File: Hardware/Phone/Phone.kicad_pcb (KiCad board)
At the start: 2 copper layers, 16.5 x 1.9 mm, 24 parts, among them J1 UART, J2 JTAG, J3 USB_C_Receptacle_USB2.0_16P, U1 ESP32-S3-WROOM-1, U2 USBLC6-2SC6

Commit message: e ink is done
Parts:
- added C10: 10p, Capacitor_SMD:C_0603_1608Metric, F.Cu at (136.4, 53.5)
- added C11: 10p, Capacitor_SMD:C_0603_1608Metric, F.Cu at (136.4, 56.1)
- added C12: 10p, Capacitor_SMD:C_0603_1608Metric, F.Cu at (136.4, 58.6)
- added C13: 33p, Capacitor_SMD:C_0603_1608Metric, F.Cu at (136.4, 61.1)
- added C14: 10p, Capacitor_SMD:C_0603_1608Metric, F.Cu at (140.4, 43.5)
- added C15: 33p, Capacitor_SMD:C_0603_1608Metric, F.Cu at (140.4, 46.0)
- added C16: 10p, Capacitor_SMD:C_0603_1608Metric, F.Cu at (140.4, 48.5)
- added C17: 33p, Capacitor_SMD:C_0603_1608Metric, F.Cu at (140.4, 51.0)
- added C18: 10p, Capacitor_SMD:C_0603_1608Metric, F.Cu at (140.4, 53.5)
- added C19: 33p, Capacitor_SMD:C_0603_1608Metric, F.Cu at (140.4, 56.1)
- added C20: 10p, Capacitor_SMD:C_0603_1608Metric, F.Cu at (140.4, 58.6)
- added C21: 33p, Capacitor_SMD:C_0603_1608Metric, F.Cu at (140.4, 61.1)
- added C22: 10p, Capacitor_SMD:C_0603_1608Metric, F.Cu at (144.4, 43.5)
- added C23: 33p, Capacitor_SMD:C_0603_1608Metric, F.Cu at (144.4, 46.0)
- added C24: 100n, Capacitor_SMD:C_0603_1608Metric, F.Cu at (144.4, 48.5)
- added C25: 22p, Capacitor_SMD:C_0603_1608Metric, F.Cu at (144.4, 51.0)
- added C26: 22p, Capacitor_SMD:C_0603_1608Metric, F.Cu at (144.4, 53.5)
- added C27: 22p, Capacitor_SMD:C_0603_1608Metric, F.Cu at (144.4, 56.1)
- added C28: 1u, Capacitor_SMD:C_0603_1608Metric, F.Cu at (144.4, 58.6)
- added C29: 1nF, Capacitor_SMD:C_1206_3216Metric, F.Cu at (151.2, 78.8)
- added C30: ~, Capacitor_SMD:C_0603_1608Metric, F.Cu at (144.4, 61.1)
- added C31: ~, Capacitor_SMD:C_0603_1608Metric, F.Cu at (148.4, 43.5)
- added C32: 1uF, Capacitor_SMD:C_0603_1608Metric, F.Cu at (143.1, 87.1)
- added C33: 1uF, Capacitor_SMD:C_0603_1608Metric, F.Cu at (143.1, 89.6)
- added C34: 1uF, Capacitor_SMD:C_0603_1608Metric, F.Cu at (143.1, 92.1)
- added C35: 1uF, Capacitor_SMD:C_0603_1608Metric, F.Cu at (143.1, 94.6)
- added C36: 1uF, Capacitor_SMD:C_0603_1608Metric, F.Cu at (147.2, 87.1)
- added C37: 1uF, Capacitor_SMD:C_0603_1608Metric, F.Cu at (147.2, 89.6)
- added C38: 1uF, Capacitor_SMD:C_0603_1608Metric, F.Cu at (147.2, 92.1)
- added C39: 4u7, Capacitor_SMD:C_0603_1608Metric, F.Cu at (147.2, 94.6)
- added C40: 1uF, Capacitor_SMD:C_0603_1608Metric, F.Cu at (151.2, 87.1)
- added C41: 4u7, Capacitor_SMD:C_0603_1608Metric, F.Cu at (151.2, 89.6)
- added C5: 10uF, Capacitor_SMD:C_0603_1608Metric, F.Cu at (93.3, 111.1)
- added C6: 33p, Capacitor_SMD:C_0603_1608Metric, F.Cu at (136.4, 43.5)
- added C7: 33p, Capacitor_SMD:C_0603_1608Metric, F.Cu at (136.4, 46.0)
- added C8: 33p, Capacitor_SMD:C_0603_1608Metric, F.Cu at (136.4, 48.5)
- added C9: 10p, Capacitor_SMD:C_0603_1608Metric, F.Cu at (136.4, 51.0)
- added CARD1: ~, Felix_GSM:SIM-SMD_503960-0696, F.Cu at (124.1, 73.6)
- added D1: ~, Felix:SOD-882_L1.0-W0.6-BI, F.Cu at (151.8, 64.3)
- added D2: ~, Felix:SOD-882_L1.0-W0.6-BI, F.Cu at (151.8, 66.2)
- added D3: ~, Felix:SOD-882_L1.0-W0.6-BI, F.Cu at (151.8, 68.1)
- added D4: ~, Felix:SOD-882_L1.0-W0.6-BI, F.Cu at (151.8, 70.0)
- added D5: ESDA6V1-5W6, Package_TO_SOT_SMD:SOT-363_SC-70-6, F.Cu at (139.9, 81.9)
- added D6: ~, Felix:SOD-882_L1.0-W0.6-BI, F.Cu at (151.8, 71.9)
- added D7: D, Diode_SMD:D_SOD-123, F.Cu at (144.1, 97.6)
- added D8: D, Diode_SMD:D_SOD-123, F.Cu at (144.1, 100.9)
- added D9: D, Diode_SMD:D_SOD-123, F.Cu at (144.1, 104.3)
- added F2: 500mA PTC, Fuse:Fuse_1206_3216Metric_Pad1.42x1.75mm_HandSolder, F.Cu at (151.4, 75.5)
- added J4: Conn_Coaxial, Connector_Coaxial:U.FL_Hirose_U.FL-R-SMT-1_Vertical, F.Cu at (93.8, 104.0)
- added J5: Conn_Coaxial, Connector_Coaxial:U.FL_Hirose_U.FL-R-SMT-1_Vertical, F.Cu at (140.3, 76.9)
- added J6: Conn_01x02_Socket, Connector_PinHeader_2.54mm:PinHeader_1x02_P2.54mm_Vertical, F.Cu at (135.5, 76.2)
- added J7: USB_C_Receptacle_USB2.0_16P, Connector_USB:USB_C_Receptacle_HRO_TYPE-C-31-M-12, F.Cu at (139.0, 69.2)
- added L1: 47nH, Inductor_SMD:L_0805_2012Metric, F.Cu at (93.5, 108.4)
- added L2: 47u, Felix:IND-SMD_L4.0-W4.0 MNR4012, F.Cu at (149.8, 98.6)
- added Q1: Si1308EDL, Package_TO_SOT_SMD:SOT-323_SC-70, F.Cu at (149.2, 103.2)
- added R11: 22R, Resistor_SMD:R_0603_1608Metric, F.Cu at (148.4, 46.0)
- added R12: 22R, Resistor_SMD:R_0603_1608Metric, F.Cu at (148.4, 48.5)
- added R13: 5k1, Resistor_SMD:R_1206_3216Metric, F.Cu at (147.6, 65.0)
- added R14: 5k1, Resistor_SMD:R_1206_3216Metric, F.Cu at (147.6, 68.3)
- added R15: 1M, Resistor_SMD:R_1206_3216Metric, F.Cu at (147.6, 71.6)
- added R16: 1K, Resistor_SMD:R_0603_1608Metric, F.Cu at (148.4, 51.0)
- added R17: 5k6, Resistor_SMD:R_0603_1608Metric, F.Cu at (148.4, 53.5)
- added R18: 1K, Resistor_SMD:R_0603_1608Metric, F.Cu at (148.4, 56.1)
- added R19: 1K, Resistor_SMD:R_0603_1608Metric, F.Cu at (148.4, 58.6)
- added R20: 5k6, Resistor_SMD:R_0603_1608Metric, F.Cu at (148.4, 61.1)
- added R21: 4k7, Resistor_SMD:R_0603_1608Metric, F.Cu at (152.4, 43.5)
- added R22: 51R, Resistor_SMD:R_0603_1608Metric, F.Cu at (152.4, 46.0)
- added R23: 51R, Resistor_SMD:R_0603_1608Metric, F.Cu at (152.4, 48.5)
- added R24: 51R, Resistor_SMD:R_0603_1608Metric, F.Cu at (152.4, 51.0)
- added R25: 0R, Resistor_SMD:R_0603_1608Metric, F.Cu at (152.4, 53.5)
- added R26: 1M, Resistor_SMD:R_0603_1608Metric, F.Cu at (151.2, 92.1)
- added R27: 2R2, Resistor_SMD:R_0603_1608Metric, F.Cu at (151.2, 94.6)
- added TP1: TestPoint, TestPoint:TestPoint_Pad_D1.0mm, F.Cu at (149.9, 82.0)
- added U4: ~, Felix_GPS:GPSM-SMD_ATGM336H-TR, F.Cu at (85.6, 107.8)
- added U5: USBLC6-2SC6, Package_TO_SOT_SMD:SOT-23-6, F.Cu at (145.7, 81.5)
- added U7: ~, Felix:MIC-TH_BD4.0-P1.40_KEEG1542PBL-A, F.Cu at (145.3, 76.5)
- added U8: ~, Felix:GDEY027T91-T01 Eink Touch LONG, F.Cu at (140.4, 104.5)
- U6: value ~ -> SIM800C; footprint Felix_GPS:GPSM-SMD_ATGM336H-TR -> RF_GSM:SIMCom_SIM800C
- moved U6 64.7 mm to (124.8, 52.8)
- moved R9 41.5 mm to (62.5, 109.4)
- moved C4 41.5 mm to (95.0, 96.6)
- moved J1 41.5 mm to (68.5, 88.2)
- moved J2 41.5 mm to (68.5, 95.4)
- moved J3 41.5 mm to (98.0, 90.3)
- moved R10 41.5 mm to (62.5, 112.3)
- moved R6 41.5 mm to (106.7, 86.1)
- moved R7 41.5 mm to (106.7, 89.4)
- moved R8 41.5 mm to (106.7, 92.7)
- moved S1 41.5 mm to (78.5, 86.0)
- moved S2 41.5 mm to (86.1, 86.0)
- moved U1 41.5 mm to (84.6, 70.5)
- moved U2 41.5 mm to (79.6, 96.5)
- moved C2 41.5 mm to (111.1, 46.0)
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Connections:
- U6 pad 1: unconnected-(U6-GND-Pad1) -> Net-(U6-UART1_TXD)
- U6 pad 10: unconnected-(U6-GND-Pad10) -> Net-(D4-C)
- U6 pad 11: unconnected-(U6-RF_IN-Pad11) -> Net-(D2-C)
- U6 pad 12: unconnected-(U6-GND-Pad12) -> Net-(D1-A)
- U6 pad 13: unconnected-(U6-NC-Pad13) -> GND
- U6 pad 14: unconnected-(U6-VCC_RF-Pad14) -> Net-(CARD1-DETECT)
- U6 pad 15: unconnected-(U6-Reserved-Pad15) -> Net-(U6-SIM_DATA)
- U6 pad 16: unconnected-(U6-SDA-Pad16) -> Net-(U6-SIM_CLK)
- U6 pad 17: unconnected-(U6-SCL-Pad17) -> Net-(U6-SIM_RST)
- U6 pad 18: unconnected-(U6-Reserved-Pad18) -> Net-(CARD1-VCC)
- U6 pad 2: unconnected-(U6-TXD-Pad2) -> Net-(U6-UART1_RXD)
- U6 pad 6: unconnected-(U6-VBAT-Pad6) -> Net-(U6-UART1_DTR)
- U6 pad 8: unconnected-(U6-VCC-Pad8) -> GND
- U6 pad 9: unconnected-(U6-NRESET-Pad9) -> Net-(D3-A)

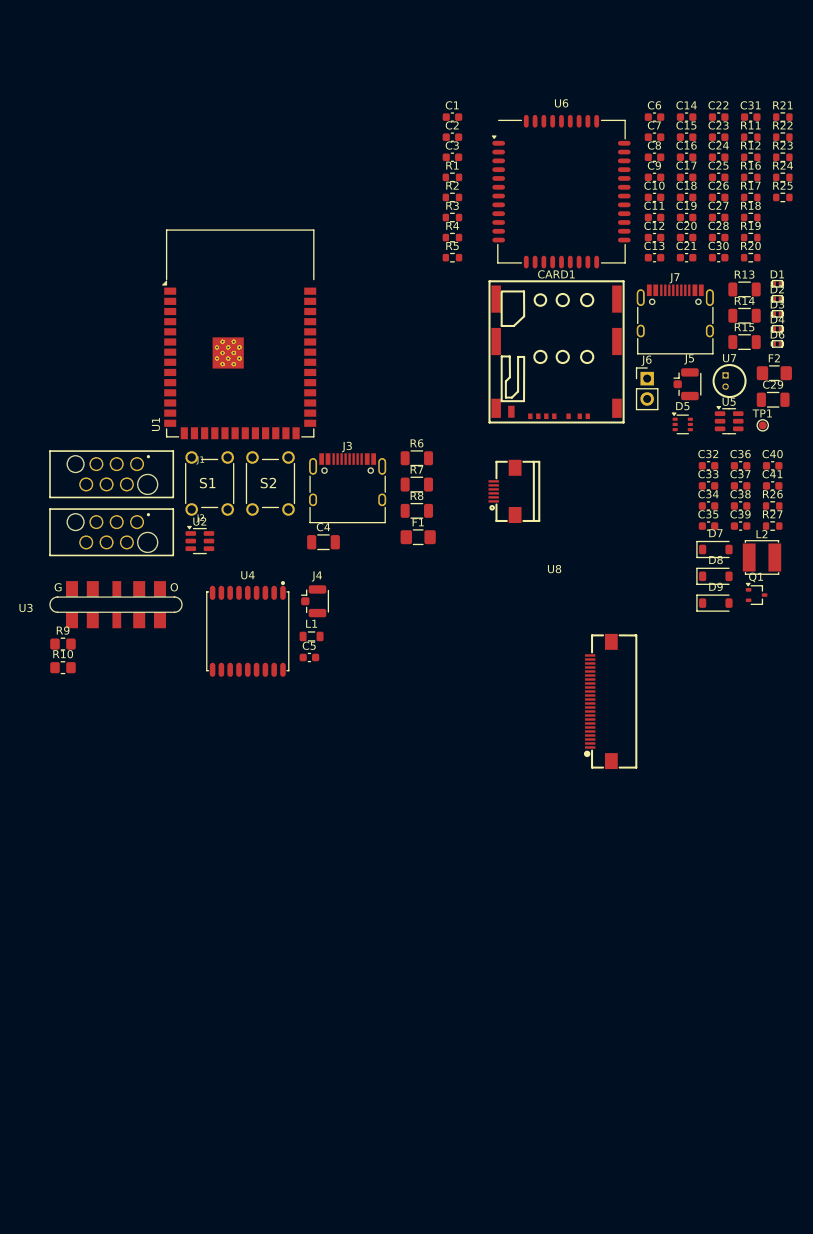
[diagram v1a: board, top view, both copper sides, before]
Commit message: phone design is done abendoning projekt
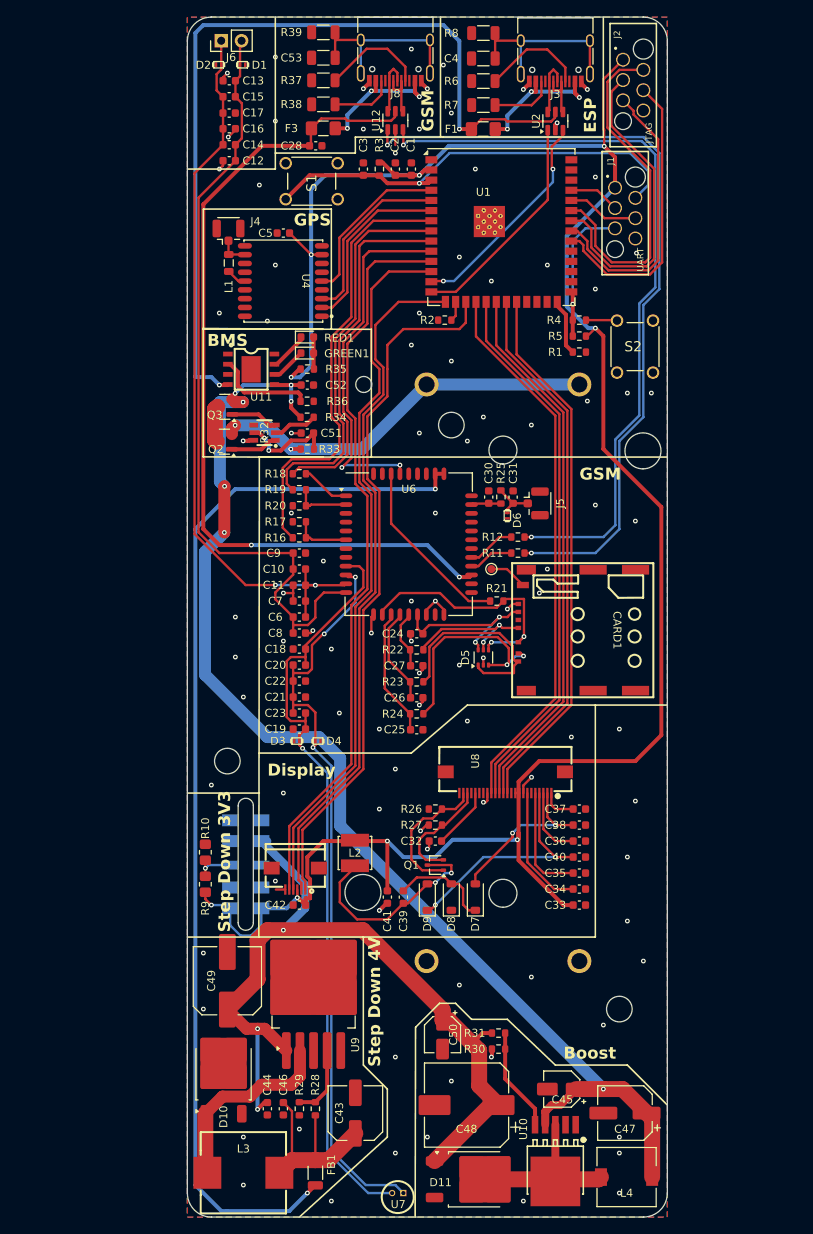
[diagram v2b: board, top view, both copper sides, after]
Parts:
- removed C29: 1nF, Capacitor_SMD:C_1206_3216Metric
- removed F2: 500mA PTC, Fuse:Fuse_1206_3216Metric_Pad1.42x1.75mm_HandSolder
- removed J7: USB_C_Receptacle_USB2.0_16P, Connector_USB:USB_C_Receptacle_HRO_TYPE-C-31-M-12
- removed R13, R14: 5k1, Resistor_SMD:R_1206_3216Metric
- removed R15: 1M, Resistor_SMD:R_1206_3216Metric
- removed U5: USBLC6-2SC6, Package_TO_SOT_SMD:SOT-23-6
- added BAT1: ~, Felix:BAT-TH_L77.0-W39.9_BH-18650-A1BJ021, B.Cu at (117.5, 113.0)
- added C42: 1uF, Capacitor_SMD:C_0603_1608Metric, F.Cu at (92.0, 142.0)
- added C43: 330u, Capacitor_SMD:C_Elec_6.3x7.7, F.Cu at (99.0, 168.0)
- added C44: 1u, Capacitor_SMD:C_0603_1608Metric, F.Cu at (88.0, 167.5)
- added C45: 10uF, Capacitor_SMD:CP_Elec_4x5.4, F.Cu at (124.8, 165.0)
- added C46: 100n, Capacitor_SMD:C_0603_1608Metric, F.Cu at (90.0, 167.5)
- added C47: 47uF, Capacitor_SMD:CP_Elec_6.3x7.7, F.Cu at (132.7, 168.0)
- added C48: 22uF, Capacitor_SMD:CP_Elec_10x10, F.Cu at (112.9, 167.0)
- added C49: 100u, Capacitor_SMD:C_Elec_8x10.2, F.Cu at (83.0, 151.5)
- added C50: 10uF, Capacitor_SMD:CP_Elec_4x5.4, F.Cu at (109.9, 158.2)
- added C51: 0u1, Capacitor_SMD:C_0603_1608Metric, F.Cu at (93.0, 83.0)
- added C52: 10uF, Capacitor_SMD:C_0603_1608Metric, F.Cu at (93.0, 77.0)
- added C53: 1nF, Capacitor_SMD:C_1206_3216Metric, F.Cu at (95.0, 36.1)
- added D10: MBR360, Package_TO_SOT_SMD:TO-252-2, F.Cu at (82.5, 163.0)
- added D11: MBR360, Package_TO_SOT_SMD:TO-252-2, F.Cu at (113.9, 176.3)
- added F3: 2A PTC, Fuse:Fuse_1206_3216Metric_Pad1.42x1.75mm_HandSolder, F.Cu at (95.0, 44.9)
- added FB1: FerriteBead 270R @ 100Mhz, Inductor_SMD:L_1206_3216Metric, F.Cu at (94.0, 175.5)
- added GREEN1: LED, LED_SMD:LED_0603_1608Metric, F.Cu at (93.0, 73.0)
- added H3: MountingHole, MountingHole:MountingHole_3.2mm_M3, F.Cu at (83.0, 124.0)
- added H4: MountingHole, MountingHole:MountingHole_3.2mm_M3, F.Cu at (111.0, 82.0)
- added H5: MountingHole, MountingHole:MountingHole_3.2mm_M3, F.Cu at (132.0, 155.0)
- added J8: USB_C_Receptacle_USB2.0_16P, Connector_USB:USB_C_Receptacle_HRO_TYPE-C-31-M-12, F.Cu at (104.0, 34.9)
- added L3: 100u, Felix:IND-SMD_L10.6-W10.2 2A 11x10mm, F.Cu at (85.0, 175.5)
- added L4: 33u, Inductor_SMD:L_7.3x7.3_H4.5, F.Cu at (132.9, 176.0)
- added Q2: AO3400A, Package_TO_SOT_SMD:SOT-23, F.Cu at (82.6, 84.1)
- added Q3: AO3400A, Package_TO_SOT_SMD:SOT-23, F.Cu at (82.7, 79.7)
- added R28: 2k2, Resistor_SMD:R_0603_1608Metric, F.Cu at (94.0, 167.5)
- added R29: 1k, Resistor_SMD:R_0603_1608Metric, F.Cu at (92.0, 167.5)
- added R30: 1k, Resistor_SMD:R_0603_1608Metric, F.Cu at (116.9, 160.0)
- added R31: 8k2, Resistor_SMD:R_0603_1608Metric, F.Cu at (116.9, 158.0)
- added R32: ~, Felix:SOT-23-6_L2.9-W1.6-P0.95-LS2.8-BR FM2113, F.Cu at (87.7, 83.0)
- added R33: 100R, Resistor_SMD:R_0603_1608Metric, F.Cu at (93.0, 85.0)
- added R34: 2K, Resistor_SMD:R_0603_1608Metric, F.Cu at (93.0, 81.0)
- added R35: 2K, Resistor_SMD:R_0603_1608Metric, F.Cu at (93.0, 75.0)
- added R36: 1K, Resistor_SMD:R_0603_1608Metric, F.Cu at (93.0, 79.0)
- added R37: 5k1, Resistor_SMD:R_1206_3216Metric, F.Cu at (95.0, 38.9)
- added R38: 5k1, Resistor_SMD:R_1206_3216Metric, F.Cu at (95.0, 41.9)
- added R39: 1M, Resistor_SMD:R_1206_3216Metric, F.Cu at (95.0, 32.9)
- added RED1: LED, LED_SMD:LED_0603_1608Metric, F.Cu at (93.0, 71.0)
- added U10: ~, Felix:TO-252-5_L6.6-W5.8-P1.27-TL XL6008E1, F.Cu at (124.0, 173.0)
- added U11: ~, Felix:ESOP-8_L4.9-W3.9-P1.27-LS6.0-BL-EP, F.Cu at (86.0, 75.0)
- added U12: USBLC6-2SC6, Package_TO_SOT_SMD:SOT-23-6, F.Cu at (104.0, 43.9)
- added U9: LM2596S-ADJ, Package_TO_SOT_SMD:TO-263-5_TabPin3, F.Cu at (93.8, 152.5)
- D1, D2, D3, D4: value ~ -> H5VL10B
- F1: value 500mA PTC -> 2A PTC
- U1: footprint RF_Module:ESP32-S3-WROOM-1 -> RF_Module:ESP32-S3-WROOM-1U
- U3: moved to B.Cu
- moved U7 109.5 mm to (104.3, 178.0), turned to -90 degrees
- moved C22 87.8 mm to (92.0, 114.0), turned to 180 degrees
- moved C23 87.4 mm to (92.0, 116.0), turned to 180 degrees
- moved J2 85.9 mm to (133.7, 39.5), turned to 90 degrees
- moved R24 81.2 mm to (106.7, 118.1), turned to 180 degrees
- moved D3 80.4 mm to (91.7, 121.5)
- moved C19 80.2 mm to (92.0, 120.0), turned to 180 degrees
- moved R23 80.0 mm to (106.7, 114.1), turned to 180 degrees
- moved R22 78.7 mm to (106.7, 110.1), turned to 180 degrees
- moved C25 78.7 mm to (106.7, 120.1), turned to 180 degrees
- moved D4 77.1 mm to (94.3, 121.5)
- moved C6 76.7 mm to (92.0, 106.0), turned to 180 degrees
- moved D2 75.7 mm to (81.9, 37.0), turned to 180 degrees
- moved C21 74.7 mm to (92.0, 118.0)
- moved C18 74.4 mm to (92.0, 110.0), turned to 180 degrees
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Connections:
- net Net-(U1-IO19) renamed /USBC/D-
- net Net-(U1-IO20) renamed /USBC/D+
- net Net-(U5-VBUS) renamed /gsm/USBC1/Vout
- C41 pad 1: unconnected-(C41-Pad1) -> GND
- R11 pad 1: Net-(R11-Pad1) -> /gsm/USBC1/D+
- R12 pad 1: Net-(R12-Pad1) -> /gsm/USBC1/D-
- S1 pad 4: GND -> unconnected-(S1-NO_2-Pad4)
- U1 pad 10: unconnected-(U1-IO17-Pad10) -> /GSM-PKey
- U1 pad 11: unconnected-(U1-IO18-Pad11) -> /T-INT
- U1 pad 12: unconnected-(U1-IO8-Pad12) -> /eink Display/T-RST
- U1 pad 15: unconnected-(U1-IO3-Pad15) -> /T-SCL
- U1 pad 17: unconnected-(U1-IO9-Pad17) -> /eink Display/T-SDA
- U1 pad 18: unconnected-(U1-IO10-Pad18) -> /eink Display/D-BUSY
- U1 pad 19: unconnected-(U1-IO11-Pad19) -> /eink Display/D-RES
- U1 pad 20: unconnected-(U1-IO12-Pad20) -> /eink Display/D-Data/Command
- U1 pad 21: unconnected-(U1-IO13-Pad21) -> /eink Display/D-CS
- U1 pad 22: unconnected-(U1-IO14-Pad22) -> /eink Display/D-SCL
- U1 pad 4: unconnected-(U1-IO4-Pad4) -> /GPS_Module/On/Off
- U1 pad 5: unconnected-(U1-IO5-Pad5) -> /GPS_Module/RX
- U1 pad 6: unconnected-(U1-IO6-Pad6) -> /GPS_Module/TX
- U1 pad 7: unconnected-(U1-IO7-Pad7) -> /gsm/DTR
- U1 pad 8: unconnected-(U1-IO15-Pad8) -> /gsm/RX
- U1 pad 9: unconnected-(U1-IO16-Pad9) -> /gsm/TX
- U3 pad 1: +5V -> +12V
- U6 pad 39: /gsm/PWRKEY -> /GSM-PKey
- U8 pad 10: unconnected-(U8-RES#-Pad10) -> /eink Display/D-RES
- U8 pad 102: unconnected-(U8-INT-Pad102) -> /T-INT
- U8 pad 103: unconnected-(U8-RST-Pad103) -> /eink Display/T-RST
- U8 pad 104: unconnected-(U8-VDD-Pad104) -> +3.3V
- U8 pad 105: unconnected-(U8-SCL-Pad105) -> /T-SCL
- U8 pad 106: unconnected-(U8-SDA-Pad106) -> /eink Display/T-SDA
- U8 pad 107: unconnected-(U8-7-Pad107) -> GND
- U8 pad 108: unconnected-(U8-8-Pad108) -> GND
- U8 pad 11: /eink Display/Data/Command -> /eink Display/D-Data/Command
- U8 pad 12: /eink Display/CS -> /eink Display/D-CS
- U8 pad 25: unconnected-(U8-Pad25) -> GND
- U8 pad 26: unconnected-(U8-Pad26) -> GND
- U8 pad 9: /eink Display/BUSY -> /eink Display/D-BUSY
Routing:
- net +3.3V: track 0.00 -> 278.1 mm, vias 0 -> 9
- net /BAT/vbatOut: track 0.00 -> 157.1 mm, vias 0 -> 7
- net +4V: track 0.00 -> 134.8 mm, vias 0 -> 2
- net /gsm/USBC1/Vout: track 0.00 -> 107.3 mm, vias 0 -> 2
- net +5V: track 0.00 -> 106.2 mm, vias 0 -> 2
- net +12V: track 0.00 -> 103.6 mm, vias 0 -> 3
- net /gsm/USBC1/D+: track 0.00 -> 99.4 mm, vias 0 -> 2
- net Net-(D1-A): track 0.00 -> 98.8 mm
- net Net-(D3-A): track 0.00 -> 96.2 mm, vias 0 -> 1
- net /gsm/USBC1/D-: track 0.00 -> 94.7 mm, vias 0 -> 2
- net Net-(D4-C): track 0.00 -> 93.9 mm, vias 0 -> 3
- net Net-(D2-C): track 0.00 -> 93.1 mm, vias 0 -> 2
- net /T-INT: track 0.00 -> 92.1 mm
- net /eink Display/T-RST: track 0.00 -> 89.6 mm
- net /eink Display/T-SDA: track 0.00 -> 87.4 mm
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- added copper zone on B.Cu, net GND
- added copper zone on F.Cu, net GND
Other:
- board size 16.5 x 1.9 mm -> 60 x 150 mm
- board text added: "BMS"
- board text added: "Boost"
- board text added: "Display"
- board text added: "ESP"
- board text added: "GPS"
- board text added: "GSM"
- board text added: "Step Down 3V3"
- board text added: "Step Down 4V"

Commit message: added doku. Abendoning Projekt
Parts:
- BAT1: value ~ -> BH-18650-A1BJ021
- CARD1: value ~ -> 5039600696
- D7, D8, D9: value D -> MBR0530
- J4, J5: value Conn_Coaxial -> BWU.FL-IPEX1
- J6: value Conn_01x02_Socket -> HDR-120632ZA-3P7
- R32: value ~ -> FM2113
- U10: value ~ -> XL6008E1
- U11: value ~ -> TP4056
- U4: value ~ -> ATGM336H-5N31
- U7: value ~ -> KEEG1542PBL-A
- U8: value ~ -> AFC01-S24FCA-00 & AFC01-S06FCA-00 & GDEY027T91-T01
